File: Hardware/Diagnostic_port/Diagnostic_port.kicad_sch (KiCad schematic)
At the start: 0 parts

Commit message: Schematic ready for review
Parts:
- added J1: USB_C_Receptacle, symbol Connector:USB_C_Receptacle
- added J2, J3, J5, J6: Conn_01x02, symbol Connector_Generic:Conn_01x02
- added J4: Conn_01x04, symbol Connector_Generic:Conn_01x04
- added J7: Conn_01x03, symbol Connector_Generic:Conn_01x03
- added JP1, JP2: Jumper_2_Open, symbol Jumper:Jumper_2_Open
- added R1, R2: 120R, symbol Device:R_Small
- added TP1, TP2: TestPoint_2Pole, symbol Connector:TestPoint_2Pole
- added U1: ~, symbol stlink:ST_LINK_V3_MODS
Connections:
- new net: JP1.2 (B), R1.1
- new net: JP2.2 (B), R2.1
- new net +5V: J1.A4 (VBUS), J1.A9 (VBUS), J1.B4 (VBUS), J1.B9 (VBUS)
- new net CAN1_H: J1.A2 (TX1+), J1.B2 (TX2+), J5.1 (Pin_1), JP1.1 (A), TP1.1
- new net CAN1_L: J1.A3 (TX1-), J1.B3 (TX2-), J5.2 (Pin_2), R1.2, TP1.2
- new net CAN2_H: J1.A11 (RX2+), J1.B11 (RX1+), J6.1 (Pin_1), JP2.1 (A), TP2.1
- new net CAN2_L: J1.A10 (RX2-), J1.B10 (RX1-), J6.2 (Pin_2), R2.2, TP2.2
- new net EXT_I2C_SCLK: J2.2 (Pin_2)
- new net EXT_I2C_SDA: J2.1 (Pin_1)
- new net EXT_SPI_CLK: J4.4 (Pin_4)
- new net EXT_SPI_MISO: J4.2 (Pin_2)
- new net EXT_SPI_MOSI: J4.3 (Pin_3)
- new net EXT_UART_RX: J3.1 (Pin_1)
- new net EXT_UART_TX: J3.2 (Pin_2)
- new net GND: J1.A1 (GND), J1.A12 (GND), J1.B1 (GND), J1.B12 (GND), J1.S1 (SHIELD), J7.2 (Pin_2)
- new net SWCLK: J1.A5 (CC1), J1.B5 (CC2), J7.3 (Pin_3)
- new net SWDIO: J1.A8 (SBU1), J1.B8 (SBU2), J7.1 (Pin_1)
- new net USB_D+: J1.A6 (D+), J1.B6 (D+)
- new net USB_D-: J1.A7 (D-), J1.B7 (D-)

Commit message: Fixed all issues
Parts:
- added C1: 100n, symbol Device:C_Small
- added D1, D2: 5V, symbol Device:D_TVS
- added D3, D4: SP0502BAHT, symbol Power_Protection:SP0502BAHT
- added F1, F2: 200mA, symbol Device:Polyfuse
- added J10: Conn_01x02, Connector_Wire:SolderWire-0.1sqmm_1x02_P3.6mm_D0.4mm_OD1mm, symbol Connector_Generic:Conn_01x03
- added J11: Conn_01x02, symbol Connector_Generic:Conn_01x02
- added J8, J9: USB_A, symbol Connector:USB_A
- added R3, R4: 680R, symbol Device:R_Small
- added U2: ATA6561-GAQW-N, Package_SO:SOIC-8_3.9x4.9mm_P1.27mm, symbol Interface_CAN_LIN:MCP2562-E-MF
- J4: symbol Connector_Generic:Conn_01x04 -> Connector_Generic:Conn_01x03
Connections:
- net +5V: now also C1.1, D1.2 (A2), D2.2 (A2), F1.1, F2.1, J10.1 (Pin_1), J11.1 (Pin_1), R3.1, R4.1, U2.3 (VDD), U2.5 (Vio)
- net CAN1_H: now also U2.7 (CANH)
- net CAN1_L: now also U2.6 (CANL)
- net EXT_I2C_SCLK: now also U1.16 (Bridge_I^{2}C_SCL), R3.2, R4.2
- net EXT_I2C_SDA: now also U1.17 (Bridge_I^{2}C_SDA)
- net EXT_SPI_CLK: now also J4.3 (Pin_3), U1.7 (Bridge_SPI_CLK); no longer J4.4 (Pin_4)
- net EXT_SPI_MISO: now also J4.1 (Pin_1), U1.23 (Bridge_SPI_MISO); no longer J4.2 (Pin_2)
- net EXT_SPI_MOSI: now also J4.2 (Pin_2), U1.25 (Bridge_SPI_MOSI); no longer J4.3 (Pin_3)
- net EXT_UART_RX: now also U1.1 (Bridge_UART_RX)
- net EXT_UART_TX: now also U1.11 (Bridge_UART_TX)
- net GND: now also U1.24 (GND), U1.26 (GND), U1.27 (GND), U1.29 (GND), U1.8 (GND), C1.2, D1.1 (A1), D2.1 (A1), D3.3 (A), D4.3 (A), J11.2 (Pin_2), J8.4 (GND), J8.5 (Shield), J9.4 (GND), J9.5 (Shield), U2.2 (VSS), U2.8 (SHDN), U2.9 (PAD)
- net SWCLK: now also U1.13 (SWCLK/JCLK)
- net SWDIO: now also U1.4 (SWDIO/JTMS)
- net USB_D+: now also D3.1 (K), J8.3 (D+)
- net USB_D-: now also D3.2 (K), J8.2 (D-)
- net TARGET_CAN_TX: now reaches U1.10 (Bridge_CAN_TX)
- net TARGET_CAN_TX: now also U2.1 (TXD)
- net TARGET_CAN_RX: now reaches U1.9 (Bridge_CAN_RX)
- net TARGET_CAN_RX: now also U2.4 (RXD)
- new net DEBUGGER_USB_D+: D4.1 (K), J10.2 (Pin_2), J9.3 (D+)
- new net DEBUGGER_USB_D-: D4.2 (K), J10.3 (Pin_3), J9.2 (D-)
- new net USB_PC_VBUS: F1.2, J8.1 (VBUS)
- new net USB_PC_VBUS_2: F2.2, J9.1 (VBUS)
- no-connect marks 0 -> 30
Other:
- note added: "Exernal connectors - circumwenting the board"
- note added: "PC to debugger connector"
- note added: "PC to target connector"
- note added: "Target SWD interface"
- note added: "The ST Link v3 MODS can operate as a protocol-to-usb device"
- note added: "These pads are to crate wiring from the Debugger to the board, going around the Micro USB connector (gimela)"
- note added: "USB - C diagnostic port"
- moved on the sheet: J1, J2, J3, J5, J6, J7, JP1, JP2, R1, R2, TP1, TP2

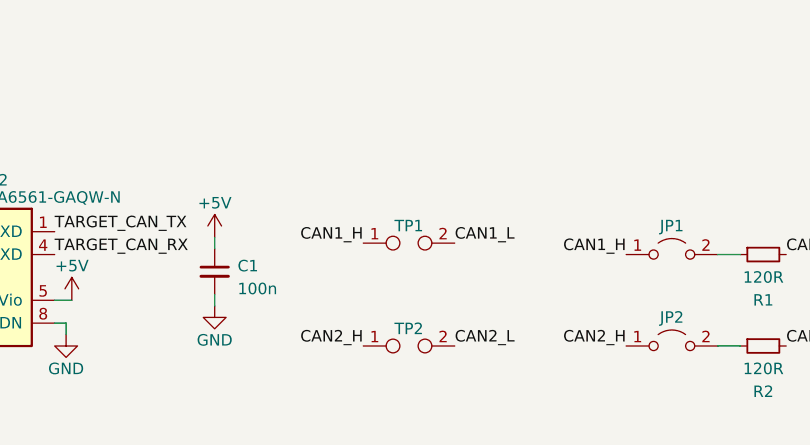
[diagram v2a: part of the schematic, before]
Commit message: Redid component placement
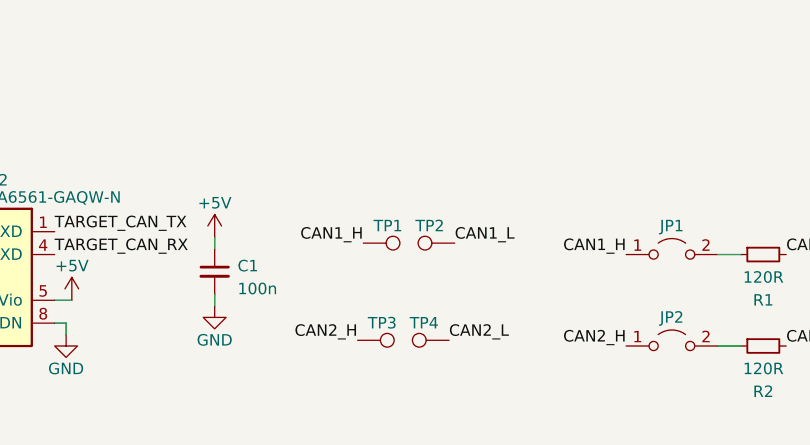
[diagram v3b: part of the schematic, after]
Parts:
- removed TP1, TP2: TestPoint_2Pole, symbol Connector:TestPoint_2Pole
- added TP1, TP2, TP3, TP4: TestPoint, symbol Connector:TestPoint
- R1, R2, R3, R4: footprint (none) -> Resistor_SMD:R_0603_1608Metric_Pad0.98x0.95mm_HandSolder
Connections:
- net CAN1_H: now also TP1.1
- net CAN1_L: now also TP2.1
- net CAN2_H: now also TP3.1
- net CAN2_L: now also TP4.1
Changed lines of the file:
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@@
     (effects (font (size 1.27 1.27)) (justify left bottom))
   )
-  (label "CAN2_L" (at 92.075 164.465 0) (fields_autoplaced)
+  (label "CAN2_L" (at 91.44 163.83 0) (fields_autoplaced)
     (effects (font (size 1.27 1.27)) (justify left bottom))
   )
@@
     (effects (font (size 1.27 1.27)) (justify right bottom))
   )
-  (label "CAN2_H" (at 81.915 164.465 180) (fields_autoplaced)
+  (label "CAN2_H" (at 81.28 163.83 180) (fields_autoplaced)
     (effects (font (size 1.27 1.27)) (justify right bottom))
   )
@@
   (label "EXT_SPI_MISO" (at 166.37 67.31 0) (fields_autoplaced)
     (effects (font (size 1.27 1.27)) (justify left bottom))
-  )
-  (symbol (lib_id "Connector:TestPoint_2Pole") (at 86.995 153.035 0) (unit 1)
-    (in_bom yes) (on_board yes) (dnp no)
-    (property "Reference" "TP1" (at 86.995 151.13 0)
-      (effects (font (size 1.27 1.27)))
-    )
-    (property "Value" "TestPoint_2Pole" (at 86.995 149.225 0)
-      (effects (font (size 1.27 1.27)) hide)
-    )
-    (property "Footprint" "" (at 86.995 153.035 0)
-      (effects (font (size 1.27 1.27)) hide)
-    )
-    (property "Datasheet" "~" (at 86.995 153.035 0)
-      (effects (font (size 1.27 1.27)) hide)
-    )
-    (pin "1")
-    (pin "2")
-    (instances
-      (project "Diagnostic_port"
-        (path "/b652b05a-4e3d-4ad1-b032-18886abe7d45"
-          (reference "TP1") (unit 1)
-        )
-      )
-    )
   )
   (symbol (lib_id "Device:C_Small") (at 65.405 156.21 0) (unit 1)
@@
     )
   )
+  (symbol (lib_id "Connector:TestPoint") (at 81.915 153.035 270) (unit 1)
+    (in_bom yes) (on_board yes) (dnp no)
+    (property "Reference" "TP1" (at 83.058 151.13 90)
+      (effects (font (size 1.27 1.27)) (justify left))
+    )
+    (property "Value" "TestPoint" (at 87.63 154.94 90)
+      (effects (font (size 1.27 1.27)) (justify left) hide)
+    )
+    (property "Footprint" "" (at 81.915 158.115 0)
+      (effects (font (size 1.27 1.27)) hide)
+    )
+    (property "Datasheet" "~" (at 81.915 158.115 0)
+      (effects (font (size 1.27 1.27)) hide)
+    )
+    (pin "1")
+    (instances
+      (project "Diagnostic_port"
+        (path "/b652b05a-4e3d-4ad1-b032-18886abe7d45"
+          (reference "TP1") (unit 1)
+        )
+      )
+    )
+  )
   (symbol (lib_id "Interface_CAN_LIN:MCP2562-E-MF") (at 34.925 156.845 0) (mirror y) (unit 1)
     (in_bom yes) (on_board yes) (dnp no)
@@
     )
   )
-  (symbol (lib_id "Connector:TestPoint_2Pole") (at 86.995 164.465 0) (unit 1)
-    (in_bom yes) (on_board yes) (dnp no)
-    (property "Reference" "TP2" (at 86.995 162.56 0)
-      (effects (font (size 1.27 1.27)))
-    )
-    (property "Value" "TestPoint_2Pole" (at 86.995 160.655 0)
-      (effects (font (size 1.27 1.27)) hide)
-    )
-    (property "Footprint" "" (at 86.995 164.465 0)
-      (effects (font (size 1.27 1.27)) hide)
-    )
-    (property "Datasheet" "~" (at 86.995 164.465 0)
-      (effects (font (size 1.27 1.27)) hide)
-    )
-    (pin "1")
-    (pin "2")
-    (instances
-      (project "Diagnostic_port"
-        (path "/b652b05a-4e3d-4ad1-b032-18886abe7d45"
-          (reference "TP2") (unit 1)
-        )
-      )
-    )
-  )
   (symbol (lib_id "power:+5V") (at 49.53 159.385 0) (unit 1)
     (in_bom yes) (on_board yes) (dnp no) (fields_autoplaced)
@@
       (effects (font (size 1.27 1.27)) (justify left))
     )
-    (property "Footprint" "" (at 151.13 19.685 0)
+    (property "Footprint" "Resistor_SMD:R_0603_1608Metric_Pad0.98x0.95mm_HandSolder" (at 151.13 19.685 0)
       (effects (font (size 1.27 1.27)) hide)
     )
@@
       (effects (font (size 1.27 1.27)))
     )
-    (property "Footprint" "" (at 126.365 164.465 0)
+    (property "Footprint" "Resistor_SMD:R_0603_1608Metric_Pad0.98x0.95mm_HandSolder" (at 126.365 164.465 0)
       (effects (font (size 1.27 1.27)) hide)
     )
@@
         (path "/b652b05a-4e3d-4ad1-b032-18886abe7d45"
           (reference "R2") (unit 1)
+        )
+      )
+    )
+  )
+  (symbol (lib_id "Connector:TestPoint") (at 81.28 163.83 270) (unit 1)
+    (in_bom yes) (on_board yes) (dnp no)
+    (property "Reference" "TP3" (at 82.423 161.925 90)
+      (effects (font (size 1.27 1.27)) (justify left))
+    )
+    (property "Value" "TestPoint" (at 86.995 165.735 90)
+      (effects (font (size 1.27 1.27)) (justify left) hide)
+    )
+    (property "Footprint" "" (at 81.28 168.91 0)
+      (effects (font (size 1.27 1.27)) hide)
+    )
+    (property "Datasheet" "~" (at 81.28 168.91 0)
+      (effects (font (size 1.27 1.27)) hide)
+    )
+    (pin "1")
+    (instances
+      (project "Diagnostic_port"
+        (path "/b652b05a-4e3d-4ad1-b032-18886abe7d45"
+          (reference "TP3") (unit 1)
         )
       )
@@
     )
   )
+  (symbol (lib_id "Connector:TestPoint") (at 92.075 153.035 90) (mirror x) (unit 1)
+    (in_bom yes) (on_board yes) (dnp no)
+    (property "Reference" "TP2" (at 90.932 151.13 90)
+      (effects (font (size 1.27 1.27)) (justify left))
+    )
+    (property "Value" "TestPoint" (at 86.36 154.94 90)
+      (effects (font (size 1.27 1.27)) (justify left) hide)
+    )
+    (property "Footprint" "" (at 92.075 158.115 0)
+      (effects (font (size 1.27 1.27)) hide)
+    )
+    (property "Datasheet" "~" (at 92.075 158.115 0)
+      (effects (font (size 1.27 1.27)) hide)
+    )
+    (pin "1")
+    (instances
+      (project "Diagnostic_port"
+        (path "/b652b05a-4e3d-4ad1-b032-18886abe7d45"
+          (reference "TP2") (unit 1)
+        )
+      )
+    )
+  )
+  (symbol (lib_id "Connector:TestPoint") (at 91.44 163.83 90) (mirror x) (unit 1)
+    (in_bom yes) (on_board yes) (dnp no)
+    (property "Reference" "TP4" (at 90.297 161.925 90)
+      (effects (font (size 1.27 1.27)) (justify left))
+    )
+    (property "Value" "TestPoint" (at 85.725 165.735 90)
+      (effects (font (size 1.27 1.27)) (justify left) hide)
+    )
+    (property "Footprint" "" (at 91.44 168.91 0)
+      (effects (font (size 1.27 1.27)) hide)
+    )
+    (property "Datasheet" "~" (at 91.44 168.91 0)
+      (effects (font (size 1.27 1.27)) hide)
+    )
+    (pin "1")
+    (instances
+      (project "Diagnostic_port"
+        (path "/b652b05a-4e3d-4ad1-b032-18886abe7d45"
+          (reference "TP4") (unit 1)
+        )
+      )
+    )
+  )
   (symbol (lib_id "Device:Polyfuse") (at 245.11 55.88 90) (unit 1)
     (in_bom yes) (on_board yes) (dnp no) (fields_autoplaced)
@@
       (effects (font (size 1.27 1.27)) (justify left))
     )
-    (property "Footprint" "" (at 142.875 19.685 0)
+    (property "Footprint" "Resistor_SMD:R_0603_1608Metric_Pad0.98x0.95mm_HandSolder" (at 142.875 19.685 0)
       (effects (font (size 1.27 1.27)) hide)
     )
@@
       (effects (font (size 1.27 1.27)))
     )
-    (property "Footprint" "" (at 126.365 154.305 0)
-      (effects (font (size 1.27 1.27)) hide)
-    )
+    (property "Footprint" "Resistor_SMD:R_0603_1608Metric_Pad0.98x0.95mm_HandSolder" (at 126.365 154.305 0)
+      (effects (font (size 1.27 1.27)) hide)
+    )

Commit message: Layout mostly done
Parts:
- removed D3, D4: SP0502BAHT, symbol Power_Protection:SP0502BAHT
- removed J11: Conn_01x02, symbol Connector_Generic:Conn_01x02
- removed TP1, TP2, TP3, TP4: TestPoint, symbol Connector:TestPoint
- added D3: 5V, Diode_SMD:D_SOD-523, symbol Device:D_TVS
- added J11, J12: Conn_01x01_Pin, Connector_Wire:SolderWirePad_1x01_SMD_5x10mm, symbol Connector:Conn_01x01_Pin
- added U3, U4: USBLC6-2P6, Package_TO_SOT_SMD:SOT-666, symbol Power_Protection:USBLC6-2P6
- C1: footprint (none) -> Capacitor_SMD:C_0402_1005Metric_Pad0.74x0.62mm_HandSolder
- D1, D2: footprint (none) -> Diode_SMD:D_SOD-523
- F1, F2: footprint (none) -> Fuse:Fuse_0603_1608Metric_Pad1.05x0.95mm_HandSolder
- J1: footprint (none) -> frontbox:CUI_UJ31-CH-31-SMT-TR
- J10: footprint Connector_Wire:SolderWire-0.1sqmm_1x02_P3.6mm_D0.4mm_OD1mm -> Connector_PinSocket_2.54mm:PinSocket_1x03_P2.54mm_Vertical
- J2, J3, J5, J6, JP1, JP2: footprint (none) -> Connector_PinHeader_2.54mm:PinHeader_1x02_P2.54mm_Vertical
- J4, J7: footprint (none) -> Connector_PinHeader_2.54mm:PinHeader_1x03_P2.54mm_Vertical
- J8, J9: footprint (none) -> Diag_port:UP2-AH-TH
- U1: footprint (none) -> Diag_port:MODULE_STLINK-V3MODS
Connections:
- net +5V: now also D3.2 (A2), J11.1 (Pin_1), U3.5 (VBUS), U4.5 (VBUS); no longer D1.2 (A2), D2.2 (A2)
- net DEBUGGER_USB_D+: now also J10.3 (Pin_3), U4.1 (I/O1); no longer J10.2 (Pin_2), J9.3 (D+)
- net DEBUGGER_USB_D-: now also J10.2 (Pin_2), U4.3 (I/O2); no longer J10.3 (Pin_3), J9.2 (D-)
- net EXT_I2C_SCLK: no longer R4.2
- net EXT_I2C_SDA: now also R4.2
- net GND: now also D3.1 (A1), J12.1 (Pin_1), U3.2 (GND), U4.2 (GND)
- net USB_D+: now also U3.1 (I/O1); no longer J8.3 (D+)
- net USB_D-: now also U3.3 (I/O2); no longer J8.2 (D-)
- net USB_PC_VBUS: now also D2.2 (A2)
- net USB_PC_VBUS_2: now also D1.2 (A2)
- new net USB_HOST+: J8.3 (D+), U3.6 (I/O1)
- new net USB_HOST-: J8.2 (D-), U3.4 (I/O2)
- new net USB_TO_DEBUGGER+: J9.3 (D+), U4.6 (I/O1)
- new net USB_TO_DEBUGGER-: J9.2 (D-), U4.4 (I/O2)
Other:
- moved on the sheet: C1, D1, D2, F1, F2, J10, J5, J6, J9, JP1, JP2, R1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
